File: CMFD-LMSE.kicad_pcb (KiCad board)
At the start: 4 copper layers, 100 x 80 mm, 130 parts, among them J1 Conn_01x02, J10 Conn_01x02, J11 Conn_01x02, J12 Conn_01x02, J2 Conn_01x02, J3 ZX62-B-5PA_33_, J4 Conn_01x02, J5 Conn_01x05, J6 Conn_01x02, J7 Conn_01x02, J8 Conn_01x02, J9 Conn_01x02, SW3 SW_SPDT, SW4 SW_Push, U1 MPM3610GQV-Z, U2 CH340E, U4 TPS2117DRLR, U5 BD33IC0WEFJ-E2, U6 MCP2562FD-H/SN, U7 STM32H503CBTx, X1 MU00525-32.768K

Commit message: 7/2 終了
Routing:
- net Net-(U1-AAM): track 0.29 -> 1.85 mm
- net Net-(U1-FB): track 7.27 -> 5.73 mm, vias 3 -> 1
- net GND: track 17.7 -> 17.9 mm, vias 8 -> 6
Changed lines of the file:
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@@
 		(capping no)
 		(filling no)
-		(zone_defaults)
 		(pcbplotparams
 			(layerselection 0x00000000_00000000_55555555_5755f5ff)
@@
 			)
 		)
-		(group ""
-			(members "0058402f-c48c-44d2-bf61-ce57f9dfae6d" "120edbcd-e95b-4c23-bb31-a7c274ccf5e6"
-				"5e9aba25-2c79-40f5-adc9-1cff49158fd8" "68b3e6a0-8775-49e5-92b8-c15adf9e5829"
-			)
-		)
 		(embedded_fonts no)
 	)
@@
 	)
 	(segment
-		(start 121.8977 108.75)
-		(end 121.8977 108.7023)
-		(width 0.7)
-		(layer "F.Cu")
-		(net "GND")
-	)
-	(segment
 		(start 110.25 104.25)
 		(end 110.975 104.975)
@@
 	)
 	(segment
-		(start 121.8977 109.65)
-		(end 121.8977 108.75)
-		(width 0.7)
+		(start 121.9 108.85)
+		(end 121.8977 108.8523)
+		(width 0.6)
 		(layer "F.Cu")
 		(net "GND")
@@
 	)
 	(segment
+		(start 121.9 108.45)
+		(end 121.9 108.85)
+		(width 0.6)
+		(layer "F.Cu")
+		(net "GND")
+	)
+	(segment
 		(start 115 108.75)
 		(end 112.975 108.75)
@@
 	)
 	(segment
-		(start 113.0375 112.8)
-		(end 113.0375 114.4)
-		(width 0.7)
+		(start 121.8977 108.8523)
+		(end 121.8977 109.65)
+		(width 0.6)
 		(layer "F.Cu")
 		(net "GND")
 	)
 	(segment
-		(start 121.8977 108.7023)
-		(end 121.9 108.7)
+		(start 113.0375 112.8)
+		(end 113.0375 114.4)
 		(width 0.7)
 		(layer "F.Cu")
@@
 	)
 	(via
-		(at 120.2125 114.4)
-		(size 0.6)
-		(drill 0.4)
-		(layers "F.Cu" "B.Cu")
-		(net "GND")
-	)
-	(via
-		(at 113.0375 114.4)
-		(size 0.6)
-		(drill 0.3)
-		(layers "F.Cu" "B.Cu")
-		(net "GND")
-	)
-	(via
 		(at 112.75 135.9)
 		(size 0.6)
@@
 	)
 	(via
-		(at 121.8977 108.75)
+		(at 110.25 104.25)
 		(size 0.6)
 		(drill 0.3)
@@
 	)
 	(via
-		(at 110.25 104.25)
+		(at 110.975 104.975)
 		(size 0.6)
 		(drill 0.3)
@@
 	)
 	(via
-		(at 110.975 104.975)
+		(at 121.9 108.45)
 		(size 0.6)
 		(drill 0.3)
@@
 	)
 	(segment
-		(start 114.1 106.75)
-		(end 115.4 106.75)
-		(width 0.4)
+		(start 115.45 106.8)
+		(end 115.912 106.8)
+		(width 0.2)
 		(layer "F.Cu")
 		(net "/PowerAndUSB/VIN_5V")
 	)
 	(segment
-		(start 115.4 106.75)
-		(end 115.45 106.8)
+		(start 114.1 106.75)
+		(end 115.4 106.75)
 		(width 0.4)
 		(layer "F.Cu")
@@
 	)
 	(segment
-		(start 115.45 106.8)
-		(end 115.912 106.8)
-		(width 0.2)
-		(layer "F.Cu")
-		(net "/PowerAndUSB/VIN_5V")
-	)
-	(segment
 		(start 114.65 106.75)
 		(end 115.450001 105.949999)
@@
 	)
 	(segment
-		(start 115.45 106.8)
-		(end 115.5 106.8)
+		(start 114.1 106.45)
+		(end 115.45 105.1)
 		(width 0.4)
 		(layer "F.Cu")
@@
 	)
 	(segment
-		(start 114.1 106.45)
-		(end 115.45 105.1)
+		(start 114.1 106.75)
+		(end 114.65 106.75)
 		(width 0.4)
 		(layer "F.Cu")
@@
 	)
 	(segment
-		(start 114.1 106.75)
-		(end 114.65 106.75)
+		(start 115.4 106.75)
+		(end 115.45 106.8)
 		(width 0.4)
 		(layer "F.Cu")
@@
 	)
 	(segment
-		(start 120.9523 108.7477)
-		(end 120.95 108.75)
-		(width 0.4)
+		(start 120.5 107.3)
+		(end 120.9523 107.3)
+		(width 0.2)
 		(layer "F.Cu")
 		(net "Net-(U1-FB)")
 	)
 	(segment
-		(start 118.898 108.75)
-		(end 119.55 108.75)
-		(width 0.4)
+		(start 121 107.3)
+		(end 121 107.4143)
+		(width 0.7)
 		(layer "F.Cu")
 		(net "Net-(U1-FB)")
 	)
 	(segment
-		(start 120.9523 107.3)
-		(end 120.9523 108.7477)
-		(width 0.4)
+		(start 120.25 107.55)
+		(end 120.25 105.8875)
+		(width 0.2)
 		(layer "F.Cu")
 		(net "Net-(U1-FB)")
 	)
 	(segment
-		(start 121 107.3)
-		(end 121 107.4143)
-		(width 0.7)
+		(start 119.5 108.75)
+		(end 120.25 108)
+		(width 0.2)
 		(layer "F.Cu")
 		(net "Net-(U1-FB)")
 	)
 	(segment
-		(start 120.35 105.7875)
+		(start 120.25 105.8875)
 		(end 120.8375 105.3)
-		(width 0.4)
+		(width 0.2)
 		(layer "F.Cu")
 		(net "Net-(U1-FB)")
 	)
 	(segment
-		(start 120.35 108.75)
-		(end 120.35 105.7875)
-		(width 0.4)
+		(start 120.25 107.55)
+		(end 120.5 107.3)
+		(width 0.2)
 		(layer "F.Cu")
 		(net "Net-(U1-FB)")
 	)
-	(via
-		(at 119.55 108.75)
-		(size 0.3)
-		(drill 0.2)
-		(layers "F.Cu" "B.Cu")
+	(segment
+		(start 118.898 108.75)
+		(end 119.5 108.75)
+		(width 0.2)
+		(layer "F.Cu")
 		(net "Net-(U1-FB)")
 	)
-	(via
-		(at 120.35 108.75)
-		(size 0.3)
-		(drill 0.2)
-		(layers "F.Cu" "B.Cu")
+	(segment
+		(start 120.25 107.55)
+		(end 120.25 108)
+		(width 0.2)
+		(layer "F.Cu")
+		(net "Net-(U1-FB)")
+	)
+	(segment
+		(start 120.25 108)
+		(end 120.25 108.05)
+		(width 0.2)
+		(layer "F.Cu")
 		(net "Net-(U1-FB)")
 	)
 	(via
-		(at 120.95 108.75)
-		(size 0.3)
-		(drill 0.2)
+		(at 120.25 108)
+		(size 0.6)
+		(drill 0.3)
 		(layers "F.Cu" "B.Cu")
 		(net "Net-(U1-FB)")
 	)
 	(segment
-		(start 119.55 108.75)
-		(end 120.35 108.75)
-		(width 0.4)
+		(start 119.65 108.75)
+		(end 119.65 108.6)
+		(width 0.2)
 		(layer "B.Cu")
 		(net "Net-(U1-FB)")
 	)
 	(segment
-		(start 120.35 108.75)
-		(end 120.95 108.75)
+		(start 121.6477 111.5)
+		(end 121.6477 111.0477)
 		(width 0.4)
-		(layer "B.Cu")
-		(net "Net-(U1-FB)")
-	)
-	(segment
-		(start 121.5 110.5)
-		(end 121.5 111.3523)
-		(width 0.32)
 		(layer "F.Cu")
 		(net "Net-(U1-EN)")
@@
 	(segment
 		(start 118.254001 109.644)
-		(end 118.254001 110.254001)
-		(width 0.2)
-		(layer "F.Cu")
-		(net "Net-(U1-EN)")
-	)
-	(segment
-		(start 118.254001 110.254001)
-		(end 118.5 110.5)
+		(end 118.254001 110.054001)
 		(width 0.2)
 		(layer "F.Cu")
@@
 	)
 	(segment
-		(start 118.5 110.5)
-		(end 119 110.5)
-		(width 0.32)
+		(start 121.6477 111.0477)
+		(end 121.2 110.6)
+		(width 0.4)
 		(layer "F.Cu")
 		(net "Net-(U1-EN)")
 	)
 	(segment
-		(start 121.5 111.3523)
-		(end 121.6477 111.5)
-		(width 0.32)
+		(start 118.254001 110.054001)
+		(end 118.8 110.6)
+		(width 0.2)
 		(layer "F.Cu")
 		(net "Net-(U1-EN)")
 	)
 	(via
-		(at 119 110.5)
-		(size 0.3)
-		(drill 0.2)
+		(at 118.8 110.6)
+		(size 0.6)
+		(drill 0.3)
 		(layers "F.Cu" "B.Cu")
 		(net "Net-(U1-EN)")
 	)
 	(via
-		(at 121.5 110.5)
-		(size 0.3)
-		(drill 0.2)
+		(at 121.2 110.6)
+		(size 0.6)
+		(drill 0.3)
 		(layers "F.Cu" "B.Cu")
 		(net "Net-(U1-EN)")
 	)
 	(segment
-		(start 119 110.5)
-		(end 121.5 110.5)
-		(width 0.32)
+		(start 121.2 110.6)
+		(end 118.8 110.6)
+		(width 0.4)
 		(layer "B.Cu")
 		(net "Net-(U1-EN)")
 	)
 	(segment
+		(start 119.044 109.644)
+		(end 119.05 109.65)
+		(width 0.2)
+		(layer "F.Cu")
+		(net "Net-(U1-AAM)")
+	)
+	(segment
 		(start 118.754 109.644)
 		(end 119.044 109.644)
 		(width 0.2)
 		(layer "F.Cu")
+		(net "Net-(U1-AAM)")
+	)
+	(segment
+		(start 119.05 109.65)
+		(end 120.6023 109.65)
+		(width 0.2)
+		(layer "F.Cu")

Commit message: 通信部分にちょっと手を出しました
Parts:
- moved C34 75.0 mm to (206.4, 90.3)
- moved C40 75.0 mm to (206.4, 92.0)
- moved C41 75.0 mm to (206.4, 94.8)
- moved TP2 18.9 mm to (89.0, 85.2)
- moved TP3 18.9 mm to (85.7, 85.2)
- moved C43 16.7 mm to (134.6, 94.2), turned to 180 degrees
- moved C42 16.1 mm to (134.5, 92.5), turned to 0 degrees
- moved C35 15.1 mm to (152.3, 88.5)
- moved C38 15.1 mm to (150.5, 88.6)
- moved C5 15.1 mm to (112.5, 103.5), turned to 180 degrees
- moved R29 10.3 mm to (109.2, 93.8)
- moved X1 10.1 mm to (135.3, 96.2), turned to 180 degrees
- moved TP4 9.74 mm to (120.0, 94.0)
- moved C7 9.61 mm to (110.0, 90.0)
- moved F2 9.33 mm to (103.8, 92.0)
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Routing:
- net /PowerAndUSB/VIN_5V: track 6.65 -> 66.8 mm, vias 0 -> 7
- net GND: track 17.9 -> 58.1 mm, vias 6 -> 32
- net /MCU/USART1_TX: track 0.00 -> 31.0 mm, vias 0 -> 2
- net /MCU/USART1_RX: track 0.00 -> 30.9 mm, vias 0 -> 2
- net /CAN/CAN_RX: track 0.00 -> 23.1 mm, vias 0 -> 4
- net SYS_5V: track 0.00 -> 16.8 mm, vias 0 -> 2
- net /PowerAndUSB/USB_5V: track 0.00 -> 16.1 mm, vias 0 -> 2
- net /PowerAndUSB/D-: track 0.00 -> 14.2 mm, vias 0 -> 3
- net Net-(U4-PR1): track 0.00 -> 13.4 mm, vias 0 -> 2
- net /PowerAndUSB/D+: track 0.00 -> 13.3 mm, vias 0 -> 3
- net OSC_OUT: track 0.00 -> 11.3 mm
- net /PowerAndUSB/VOTGID: track 0.00 -> 10.4 mm, vias 0 -> 2
- net OSC_IN: track 0.00 -> 10.2 mm
- net Net-(U4-ST): track 0.00 -> 10.1 mm, vias 0 -> 2
- net +3.3V: track 0.00 -> 9.43 mm, vias 0 -> 2
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- added copper zone on In1.Cu, net +3.3V
- added copper zone on In2.Cu, net GND

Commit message: 自動配線を試して見る
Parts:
- moved C41 74.8 mm to (131.8, 99.6), turned to 90 degrees
- moved C40 73.0 mm to (133.8, 99.6), turned to 90 degrees
- moved C34 67.4 mm to (139.1, 94.0)
- moved TP2 33.6 mm to (116.5, 66.0)
- moved TP3 30.6 mm to (109.4, 66.0)
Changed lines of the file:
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@@
 	(footprint "TestPoint:TestPoint_Pad_1.5x1.5mm"
 		(layer "F.Cu")
-		(at 89 85.25)
+		(at 116.5 66)
 		(descr "SMD rectangular pad as test Point, square 1.5mm side length")
 		(tags "test point SMD pad rectangle square")
@@
 	(footprint "Capacitor_SMD:C_0603_1608Metric_Pad1.08x0.95mm_HandSolder"
 		(layer "F.Cu")
-		(at 206.3875 90.35 180)
+		(at 139.1125 94 180)
 		(descr "Capacitor SMD 0603 (1608 Metric), square (rectangular) end terminal, IPC-7351 nominal with elongated pad for handsoldering. (Body size source: IPC-SM-782 page 76, https://www.pcb-3d.com/wordpress/wp-content/uploads/ipc-sm-782a_amendment_1_and_2.pdf)")
 		(tags "capacitor handsolder")
@@
 	(footprint "Capacitor_SMD:C_0603_1608Metric_Pad1.08x0.95mm_HandSolder"
 		(layer "F.Cu")
-		(at 206.3875 94.75 180)
+		(at 131.75 99.6125 90)
 		(descr "Capacitor SMD 0603 (1608 Metric), square (rectangular) end terminal, IPC-7351 nominal with elongated pad for handsoldering. (Body size source: IPC-SM-782 page 76, https://www.pcb-3d.com/wordpress/wp-content/uploads/ipc-sm-782a_amendment_1_and_2.pdf)")
 		(tags "capacitor handsolder")
 		(property "Reference" "C41"
-			(at 0 -1.43 0)
+			(at 0 -1.43 90)
 			(layer "F.SilkS")
 			(effects
@@
 		)
 		(property "Value" "0.1µF"
-			(at 0 1.43 0)
+			(at 0 1.43 90)
 			(layer "F.Fab")
 			(effects
@@
 		)
 		(property "Datasheet" ""
-			(at 0 0 0)
+			(at 0 0 90)
 			(layer "F.Fab")
 			(hide yes)
@@
 		)
 		(property "Description" "Unpolarized capacitor"
-			(at 0 0 0)
+			(at 0 0 90)
 			(layer "F.Fab")
 			(hide yes)
@@
 		)
 		(property "KiLib_Generator" "SMD_2terminal_chip_molded"
-			(at 0 0 0)
+			(at 0 0 90)
 			(layer "F.SilkS")
 			(hide yes)
@@
 		(duplicate_pad_numbers_are_jumpers no)
 		(fp_line
-			(start -0.146267 0.51)
-			(end 0.146267 0.51)
+			(start -0.146267 -0.51)
+			(end 0.146267 -0.51)
 			(stroke
 				(width 0.12)
@@
 		)
 		(fp_line
-			(start -0.146267 -0.51)
-			(end 0.146267 -0.51)
+			(start -0.146267 0.51)
+			(end 0.146267 0.51)
 			(stroke
 				(width 0.12)
@@
 		)
 		(fp_text user "${REFERENCE}"
-			(at 0 0 0)
+			(at 0 0 90)
 			(layer "F.Fab")
 			(effects
@@
 		)
 		(pad "1" smd roundrect
-			(at -0.8625 0 180)
+			(at -0.8625 0 90)
 			(size 1.075 0.95)
 			(layers "F.Cu" "F.Mask" "F.Paste")
@@
 		)
 		(pad "2" smd roundrect
-			(at 0.8625 0 180)
+			(at 0.8625 0 90)
 			(size 1.075 0.95)
 			(layers "F.Cu" "F.Mask" "F.Paste")
@@
 	(footprint "Capacitor_SMD:C_0603_1608Metric_Pad1.08x0.95mm_HandSolder"
 		(layer "F.Cu")
-		(at 206.3875 91.95 180)
+		(at 133.75 99.6125 90)
 		(descr "Capacitor SMD 0603 (1608 Metric), square (rectangular) end terminal, IPC-7351 nominal with elongated pad for handsoldering. (Body size source: IPC-SM-782 page 76, https://www.pcb-3d.com/wordpress/wp-content/uploads/ipc-sm-782a_amendment_1_and_2.pdf)")
 		(tags "capacitor handsolder")
 		(property "Reference" "C40"
-			(at 0 -1.43 0)
+			(at -0.1375 1.5 90)
 			(layer "F.SilkS")
 			(effects
@@
 		)
 		(property "Value" "1µF"
-			(at 0 1.43 0)
+			(at 0 1.43 90)
 			(layer "F.Fab")
 			(effects
@@
 		)
 		(property "Datasheet" ""
-			(at 0 0 0)
+			(at 0 0 90)
 			(layer "F.Fab")
 			(hide yes)
@@
 		)
 		(property "Description" "Unpolarized capacitor"
-			(at 0 0 0)
+			(at 0 0 90)
 			(layer "F.Fab")
 			(hide yes)
@@
 		)
 		(property "KiLib_Generator" "SMD_2terminal_chip_molded"
-			(at 0 0 0)
+			(at 0 0 90)
 			(layer "F.SilkS")
 			(hide yes)
@@
 		(duplicate_pad_numbers_are_jumpers no)
 		(fp_line
-			(start -0.146267 0.51)
-			(end 0.146267 0.51)
+			(start -0.146267 -0.51)
+			(end 0.146267 -0.51)
 			(stroke
 				(width 0.12)
@@
 		)
 		(fp_line
-			(start -0.146267 -0.51)
-			(end 0.146267 -0.51)
+			(start -0.146267 0.51)
+			(end 0.146267 0.51)
 			(stroke
 				(width 0.12)
@@
 		)
 		(fp_text user "${REFERENCE}"
-			(at 0 0 0)
+			(at 0 0 90)
 			(layer "F.Fab")
 			(effects
@@
 		)
 		(pad "1" smd roundrect
-			(at -0.8625 0 180)
+			(at -0.8625 0 90)
 			(size 1.075 0.95)
 			(layers "F.Cu" "F.Mask" "F.Paste")
@@
 		)
 		(pad "2" smd roundrect
-			(at 0.8625 0 180)
+			(at 0.8625 0 90)
 			(size 1.075 0.95)
 			(layers "F.Cu" "F.Mask" "F.Paste")
@@
 	(footprint "TestPoint:TestPoint_Pad_1.5x1.5mm"
 		(layer "F.Cu")
-		(at 85.65 85.2)
+		(at 109.4 65.95)
 		(descr "SMD rectangular pad as test Point, square 1.5mm side length")
 		(tags "test point SMD pad rectangle square")

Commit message: 電源系だいたい完了
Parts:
- moved J5 62.7 mm to (168.9, 35.5)
- moved C34 18.7 mm to (157.6, 91.2)
- moved X1 12.1 mm to (143.1, 87.0)
- moved C10 10.5 mm to (120.5, 95.5), turned to 180 degrees
- moved C41 7.68 mm to (138.1, 95.4), turned to 45 degrees
- moved C40 5.92 mm to (135.6, 94.0), turned to 180 degrees
- moved C44 5.86 mm to (144.2, 109.1), turned to -90 degrees
- moved TP4 4.78 mm to (115.2, 94.5)
- moved C36 4.39 mm to (148.0, 105.8), turned to 45 degrees
- moved C45 4.34 mm to (146.4, 92.0), turned to 180 degrees
- moved C42 3.88 mm to (135.5, 88.8)
- moved C43 3.88 mm to (135.6, 90.5)
- moved C30 1.66 mm to (133.8, 106.1), turned to -90 degrees
- moved C11 1.57 mm to (130.2, 87.0)
- moved C28 1.54 mm to (135.6, 109.0)
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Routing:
- net +3.3V: track 9.43 -> 31.1 mm, vias 2 -> 4
- net +BATT: track 0.00 -> 14.6 mm, vias 9 -> 4
- net GND: track 58.1 -> 69.4 mm, vias 32 -> 40
- net SYS_5V: track 16.8 -> 25.8 mm
- net OSC32_IN: track 8.30 -> 0.00 mm
- net OSC32_OUT: track 8.05 -> 0.00 mm
- net Net-(C45-Pad1): track 5.38 -> 0.00 mm
- net Net-(C44-Pad1): track 5.74 -> 3.76 mm, vias 2 -> 1
- net OSC_IN: track 10.2 -> 9.26 mm
- net OSC_OUT: track 11.3 -> 10.7 mm

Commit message: 0714 作業開始
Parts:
- moved J10 99.9 mm to (228.8, 45.5)
- moved J8 99.9 mm to (210.5, 45.5)
- moved J9 99.9 mm to (219.7, 45.5)
- moved J1 99.9 mm to (192.2, 45.5)
- moved J11 99.9 mm to (238.0, 45.5)
- moved J12 99.9 mm to (247.1, 45.5)
- moved J7 99.9 mm to (201.3, 45.5)
- moved J6 93.5 mm to (97.2, 83.2), turned to 180 degrees
- moved C13 69.4 mm to (102.0, 79.0), turned to 90 degrees
- moved R39 66.2 mm to (101.8, 84.8), turned to -90 degrees
- moved U6 58.6 mm to (106.2, 81.8), turned to 180 degrees
- moved C12 52.7 mm to (114.6, 80.5), turned to 0 degrees
- moved X1 14.9 mm to (132.8, 97.7), turned to -90 degrees
- moved C38 12.0 mm to (138.9, 91.5), turned to 180 degrees
- moved C43 9.08 mm to (130.5, 98.0), turned to -90 degrees
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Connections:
- C12 pad 1: +5V -> SYS_5V
- U6 pad 3: +5V -> SYS_5V
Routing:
- net /CAN/CAN_TX: track 0.00 -> 75.3 mm, vias 0 -> 2
- net /CAN/CAN_RX: track 23.1 -> 82.0 mm, vias 4 -> 2
- net SYS_5V: track 25.8 -> 52.4 mm, vias 2 -> 4
- net +3.3V: track 31.1 -> 42.4 mm, vias 4 -> 8
- net OSC32_IN: track 0.00 -> 9.71 mm
- net Net-(U4-ST): track 10.1 -> 19.3 mm, vias 2 -> 3
- net OSC32_OUT: track 0.00 -> 8.41 mm
- net GND: track 69.4 -> 77.1 mm, vias 40 -> 48
- net Net-(J6-Pin_2): track 0.00 -> 7.56 mm
- net Net-(J4-Pin_1): track 0.00 -> 7.05 mm
- net Net-(C45-Pad1): track 0.00 -> 4.93 mm
- net Net-(D17-A): track 0.00 -> 4.68 mm
- net Net-(D14-A): track 0.00 -> 4.60 mm
- net +5V: track 4.19 -> 0.00 mm

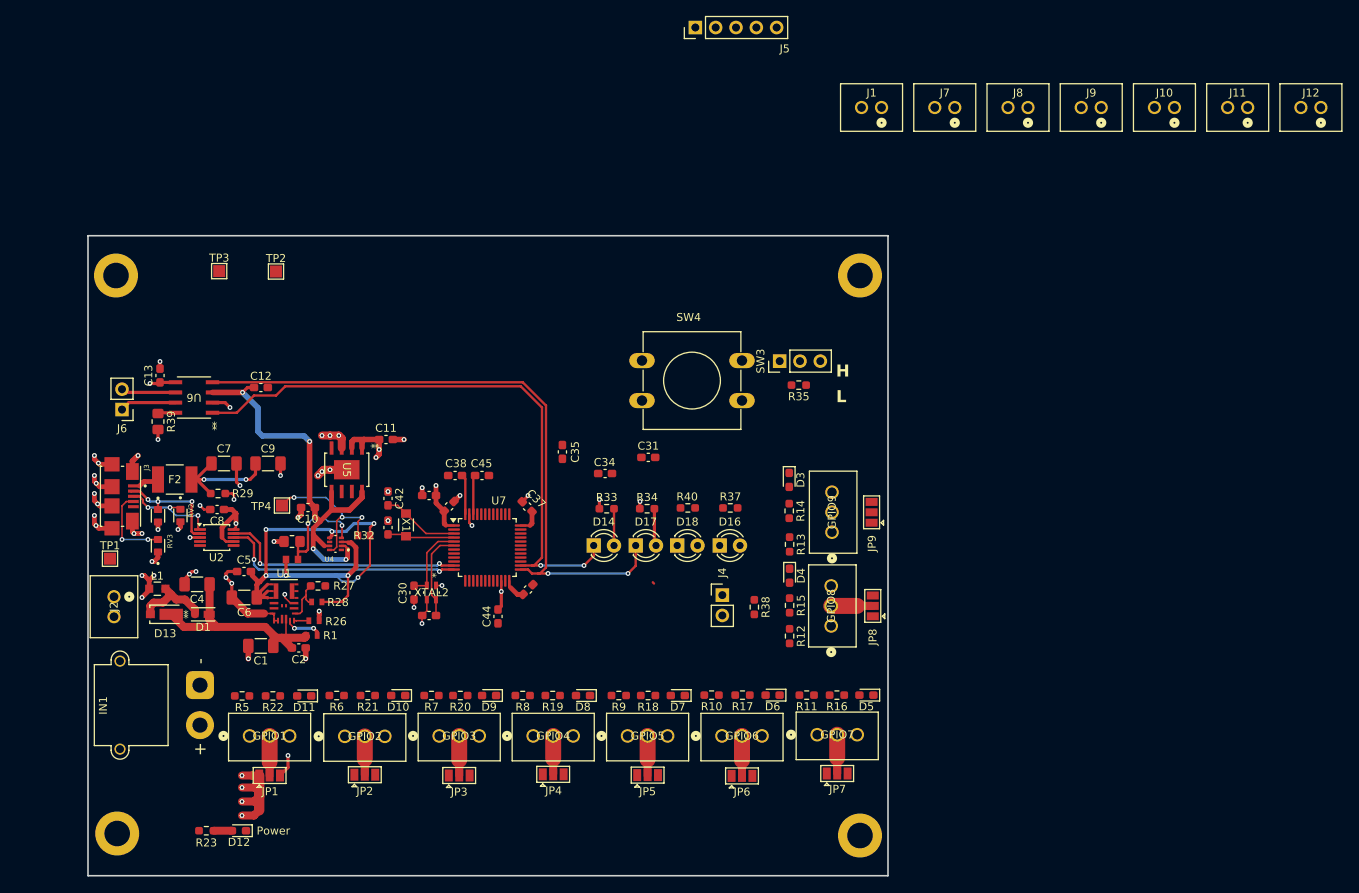
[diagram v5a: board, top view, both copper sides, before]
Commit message: サーボ電源と通信線一部
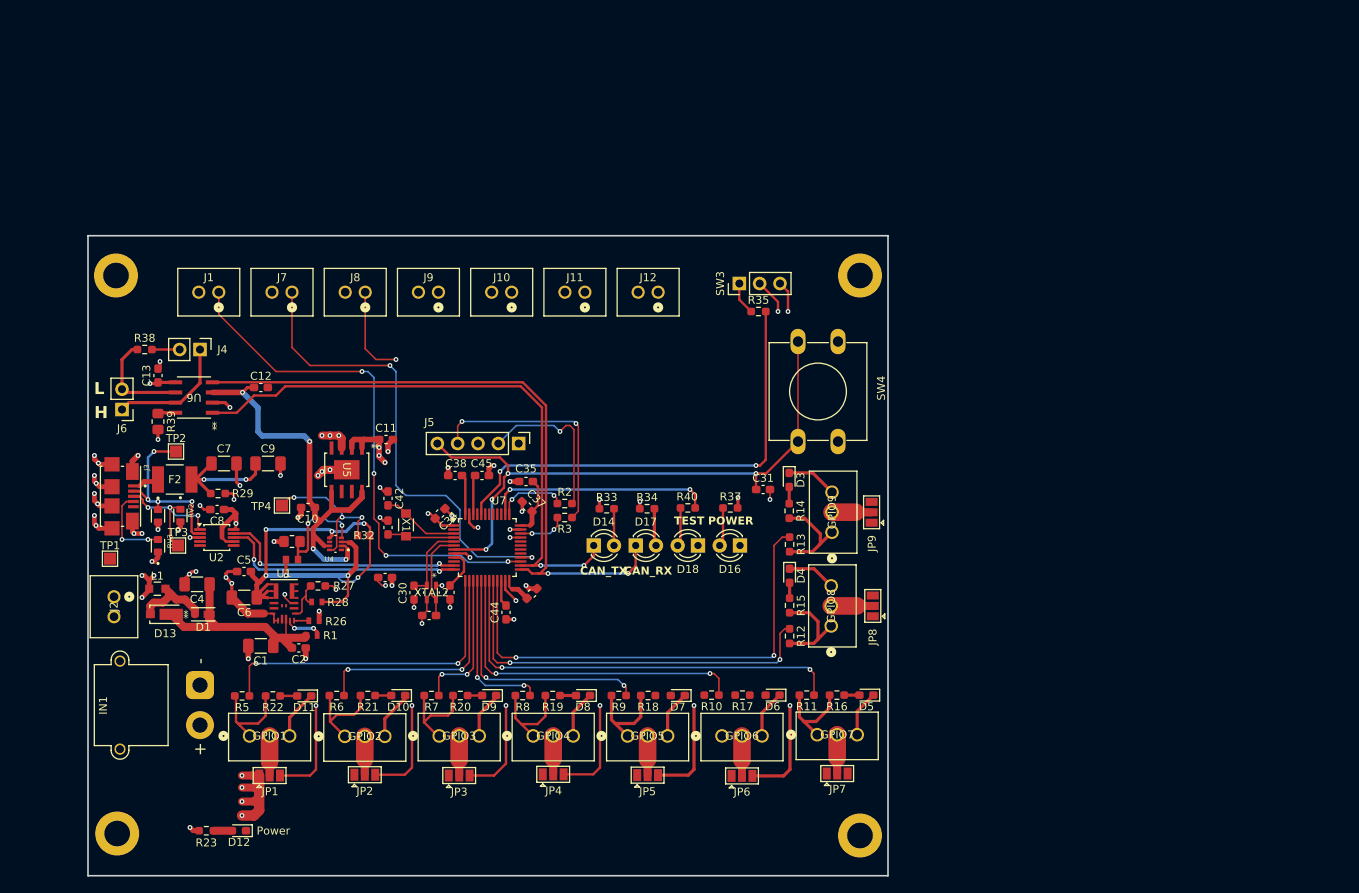
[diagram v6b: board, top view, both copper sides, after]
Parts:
- added R2: 33, Resistor_SMD:R_0603_1608Metric_Pad0.98x0.95mm_HandSolder, F.Cu at (152.6, 95.0)
- added R3: 33, Resistor_SMD:R_0603_1608Metric_Pad0.98x0.95mm_HandSolder, F.Cu at (152.6, 96.8)
- moved J10 86.0 mm to (146.0, 68.6)
- moved J1 86.0 mm to (109.3, 68.6)
- moved J11 86.0 mm to (155.1, 68.6)
- moved J12 86.0 mm to (164.3, 68.6)
- moved J7 86.0 mm to (118.5, 68.6)
- moved J8 86.0 mm to (127.7, 68.6)
- moved J9 86.0 mm to (136.8, 68.6)
- moved R38 82.7 mm to (100.1, 75.8), turned to 0 degrees
- moved J4 72.1 mm to (107.0, 75.8), turned to -90 degrees
- moved J5 56.5 mm to (146.8, 87.5), turned to -90 degrees
- moved TP3 34.7 mm to (104.2, 100.2)
- moved TP2 25.7 mm to (104.0, 88.5)
- moved SW4 24.6 mm to (186.8, 74.8), turned to -90 degrees
- moved C34 21.2 mm to (137.0, 96.2), turned to 45 degrees
- moved C31 14.9 mm to (177.4, 93.2)
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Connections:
- net /MCU/GPIO_６ renamed /MCU/GPIO_6
- J5 pad 2: /MCU/PA14-JTCK-SWCLK -> Net-(J5-Pin_2)
- J5 pad 4: /MCU/PA13-JTMS-SWDIO -> Net-(J5-Pin_4)
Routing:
- net +3.3V: track 42.4 -> 130.4 mm, vias 8 -> 17
- net GND: track 77.1 -> 156.8 mm, vias 48 -> 60
- net /MCU/NRST: track 0.00 -> 78.0 mm, vias 0 -> 4
- net /MCU/GPIO_LM_1: track 0.00 -> 65.5 mm, vias 0 -> 4
- net /MCU/GPIO_9: track 0.00 -> 60.1 mm, vias 0 -> 2
- net /MCU/GPIO_LM_2: track 0.00 -> 59.8 mm, vias 0 -> 2
- net BOOT0: track 0.00 -> 58.7 mm, vias 0 -> 2
- net /MCU/GPIO_7: track 0.00 -> 53.9 mm, vias 0 -> 2
- net /MCU/GPIO_8: track 0.00 -> 51.0 mm, vias 0 -> 2
- net /MCU/GPIO_6: track 0.00 -> 42.6 mm, vias 0 -> 2
- net /MCU/GPIO_1: track 0.00 -> 40.7 mm, vias 0 -> 2
- net /MCU/GPIO_5: track 0.00 -> 31.5 mm, vias 0 -> 2
- net Net-(J5-Pin_4): track 0.00 -> 29.5 mm, vias 0 -> 2
- net /MCU/GPIO_2: track 0.00 -> 29.3 mm, vias 0 -> 2
- net Net-(U7-PA15(JTDI)): track 0.00 -> 28.4 mm, vias 0 -> 2
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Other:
- board text added: "CAN_RX"
- board text added: "CAN_TX"
- board text added: "POWER"
- board text added: "TEST"
